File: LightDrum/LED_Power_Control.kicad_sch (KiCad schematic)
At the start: 9 parts, among them J901 DIN-4-SH, K901 ALQ112, K902 ALQ112, U902 SSM3K361R_SOT23F

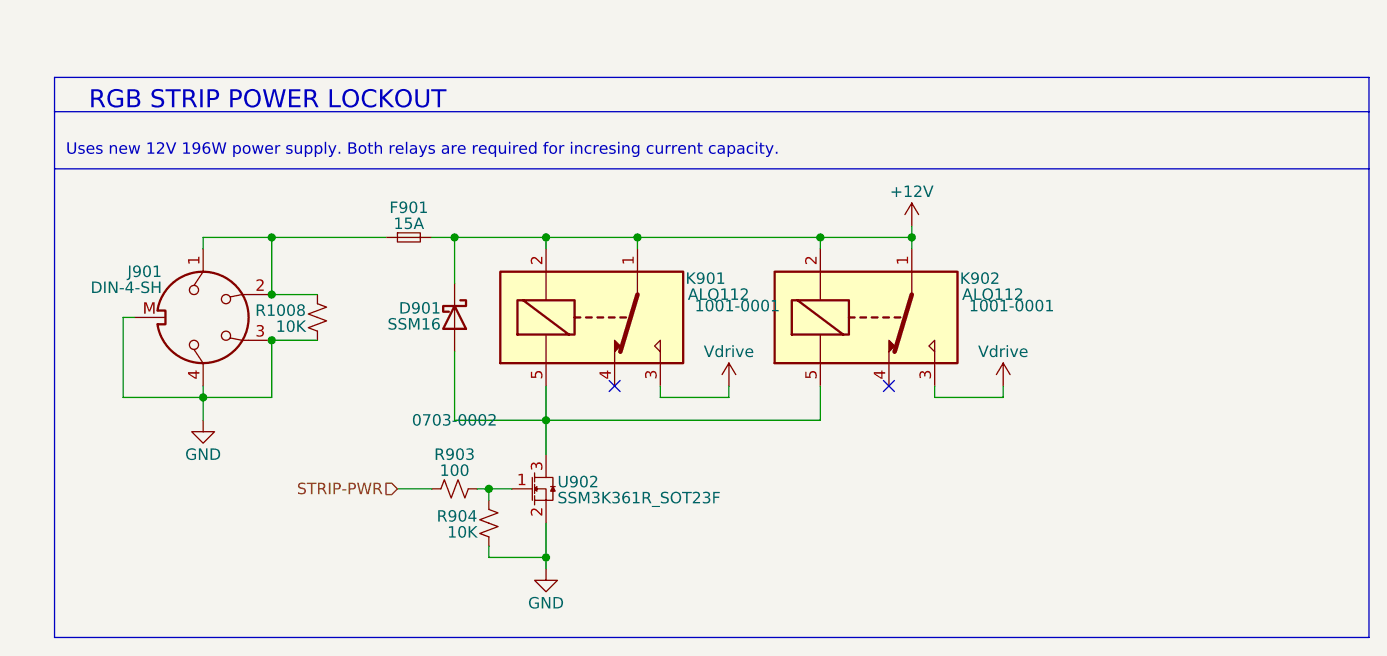
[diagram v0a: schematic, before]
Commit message: Replace relays and SWD conn
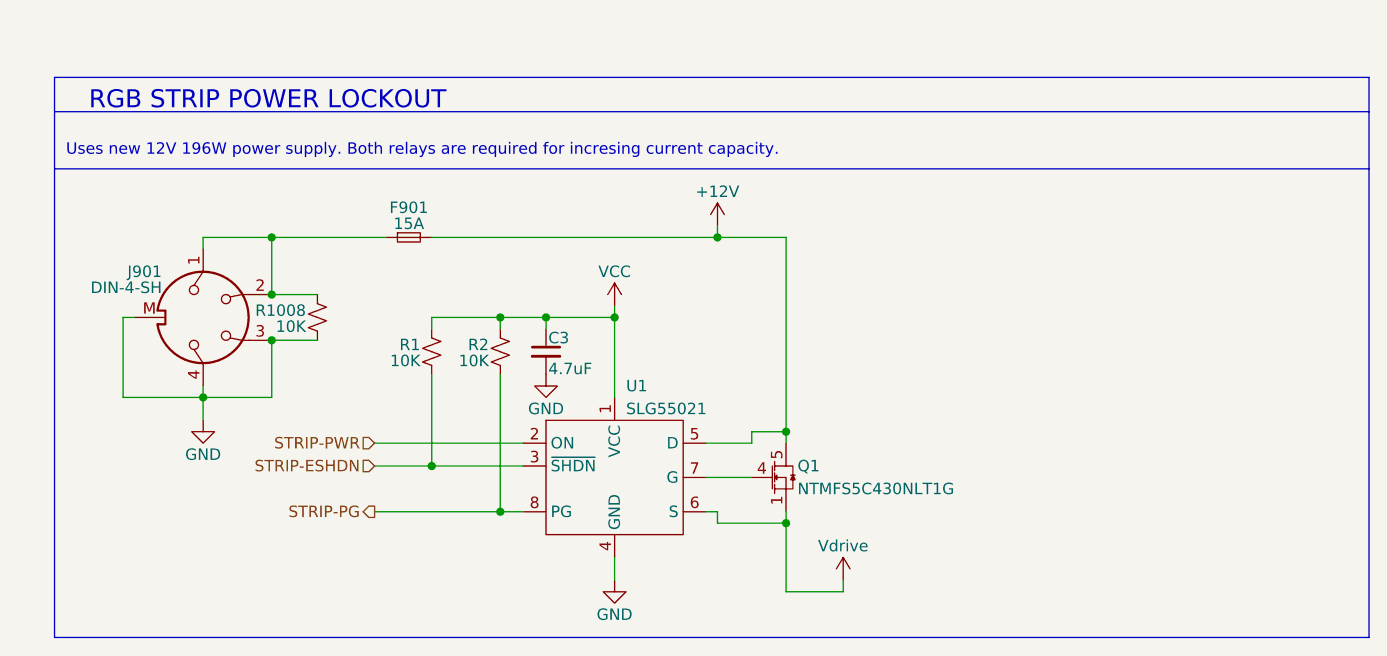
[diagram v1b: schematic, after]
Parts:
- removed D901: SSM16, Diode_SMD:D_SOD-323_HandSoldering, symbol Device:D_Schottky
- removed K901, K902: ALQ112, Daxxn_Relays:ALQ112, symbol Daxxn_Relays:ALQ112
- removed R903: 100, Resistor_SMD:R_0805_2012Metric, symbol Device:R_Small_US
- removed R904: 10K, Resistor_SMD:R_0805_2012Metric, symbol Device:R_Small_US
- removed U902: SSM3K361R_SOT23F, Package_TO_SOT_SMD:SOT-23, symbol Daxxn_Transistors:SSM3K361R_SOT23F
- added C3: 4.7uF, Capacitor_SMD:C_0805_2012Metric, symbol Daxxn_Device:C
- added Q1: NTMFS5C430NLT1G, Daxxn_Packages:POWER-FET-5-DFN, symbol Daxxn_Transistors:NTMFS5C430NL
- added R1, R2: 10K, Resistor_SMD:R_0402_1005Metric, symbol Device:R_Small_US
- added U1: SLG55021, Package_DFN_QFN:TDFN-8-1EP_2x2mm_P0.5mm_EP0.8x1.2mm, symbol Daxxn_IC:SLG55021
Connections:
- net +12V: now also Q1.5 (D), U1.5 (D)
- net GND: now also C3.2, U1.4 (GND), U1.9 (GND)
- net STRIP-PWR: now also U1.2 (ON)
- net Vdrive: now also Q1.1 (S), Q1.2 (S), Q1.3 (S), U1.6 (S)
- new net: Q1.4 (G), U1.7 (G)
- new net STRIP-ESHDN: R1.2, U1.3 (~{SHDN})
- new net STRIP-PG: R2.2, U1.8 (PG)
- new net VCC: C3.1, R1.1, R2.1, U1.1 (VCC)
- no-connect marks 2 -> 0

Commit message: Preliminary schematic lock - Starting PCB layout
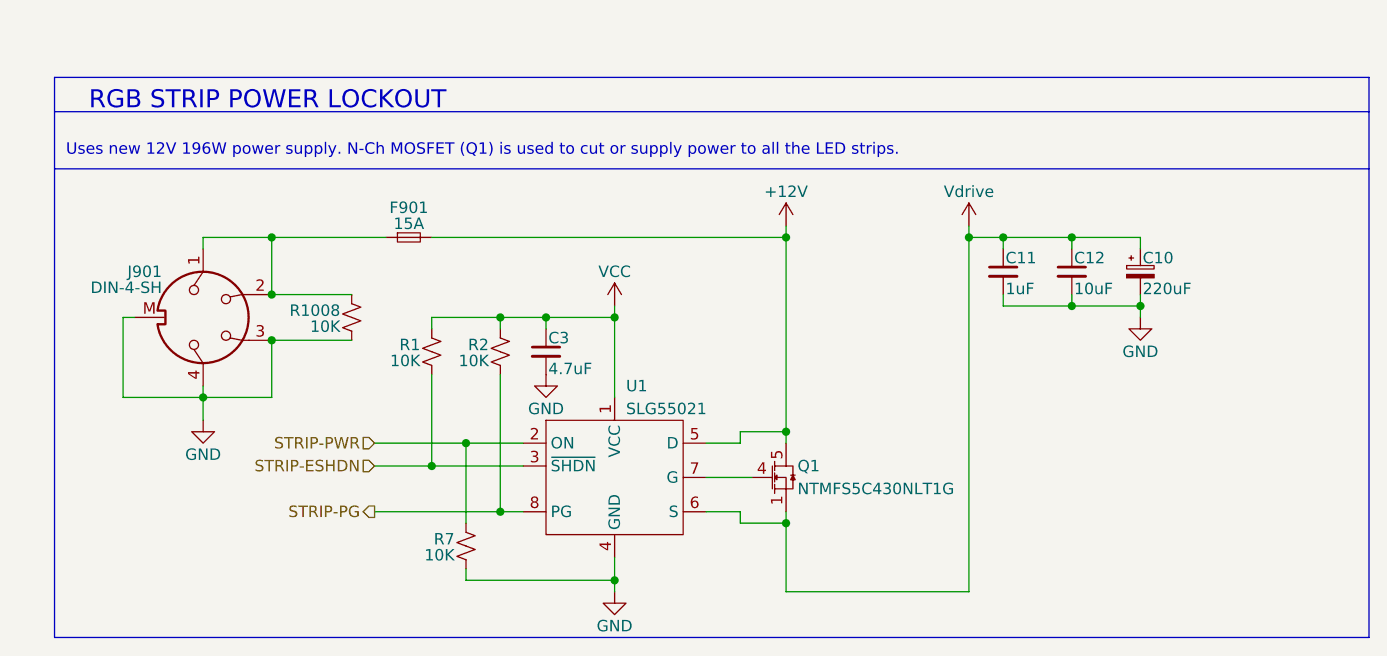
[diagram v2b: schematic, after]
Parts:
- added C10: 220uF, Capacitor_SMD:CP_Elec_8x10, symbol Daxxn_Device:C_Pol
- added C11: 1uF, Capacitor_SMD:C_0603_1608Metric, symbol Daxxn_Device:C
- added C12: 10uF, Capacitor_SMD:C_1210_3225Metric, symbol Daxxn_Device:C
- added R7: 10K, Resistor_SMD:R_0402_1005Metric, symbol Device:R_Small_US
- C3: SupplierPN (none) -> 1276-6722-1-ND
- F901: SupplierPN (none) -> 36-3557-10-ND
- J901: SupplierPN (none) -> 2092-KPJXHT-4S-S-ND
- Q1: SupplierPN (none) -> NTMFS5C430NLT1GOSCT-ND
- R1, R2: SupplierPN (none) -> 311-10KJRCT-ND
- R1008: SupplierPN (none) -> 13-RE1206FRE0710KLCT-ND
- U1: SupplierPN (none) -> 1827-1047-1-ND
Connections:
- net GND: now also C10.2, C11.2, C12.2, R7.2
- net STRIP-PWR: now also R7.1
- net Vdrive: now also C10.1, C11.1, C12.1
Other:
- note added: "Uses new 12V 196W power supply. N-Ch MOSFET (Q1) is used to cut or supply power to all the LED strips."
- note removed: "Uses new 12V 196W power supply. Both relays are required for incresing current capacity."
- moved on the sheet: R1008

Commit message: Component placement complete
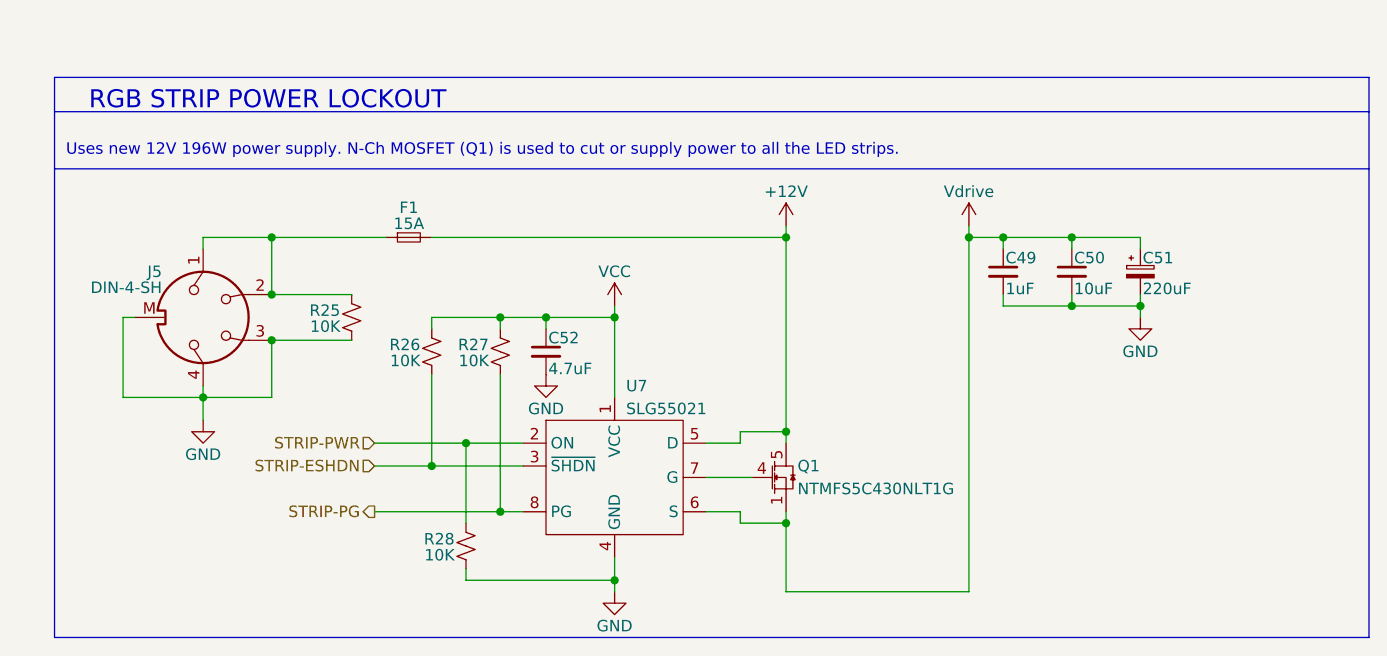
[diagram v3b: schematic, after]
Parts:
- U7: renamed from U1; footprint Package_DFN_QFN:TDFN-8-1EP_2x2mm_P0.5mm_EP0.8x1.2mm -> Daxxn_Packages:TDFN-8-1EP_2x2mm_P0.5mm_EP0.8x1.2mm
- renumbered C11 to C49, C12 to C50, C10 to C51, C3 to C52, F901 to F1, J901 to J5, R1008 to R25, R1 to R26, R2 to R27, R7 to R28

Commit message: Replace DSub with much better ECU conn
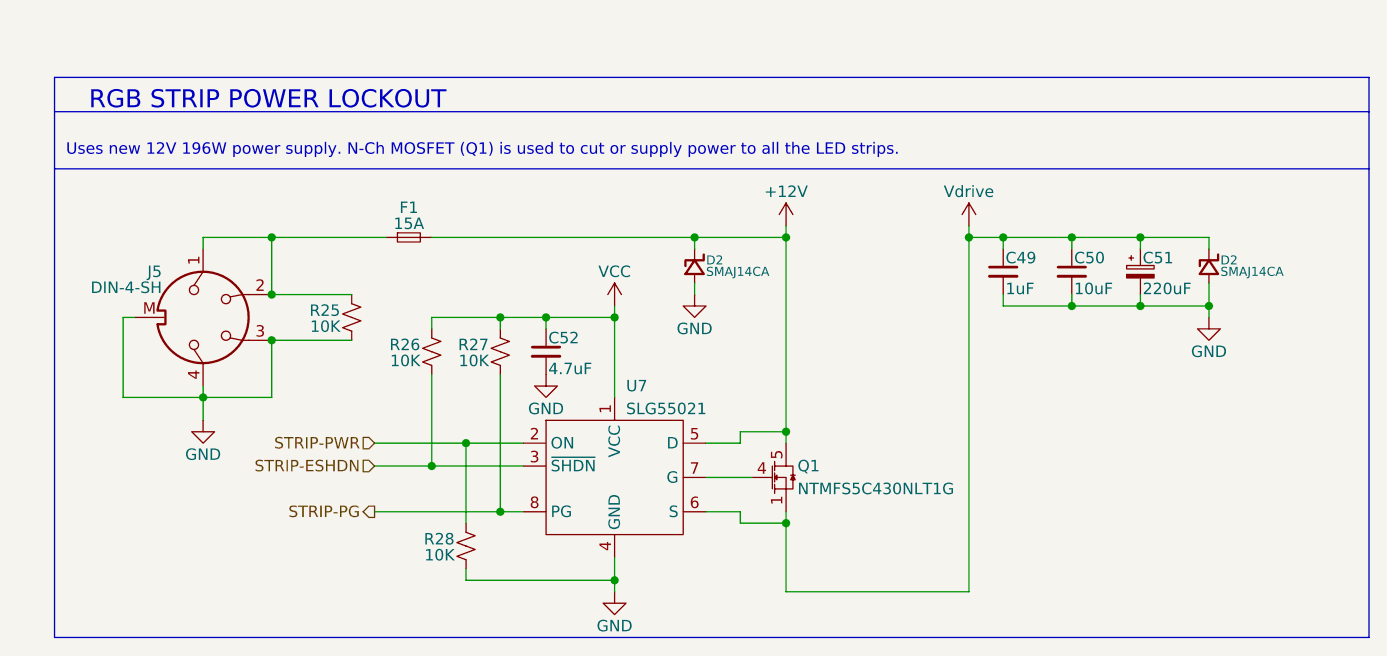
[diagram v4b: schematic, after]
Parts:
- added D2 (x2): SMAJ14CA, Diode_SMD:D_SMA, symbol Daxxn_Device:D_TVS_U
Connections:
- net +12V: now also D2.1 (K)
- net GND: now also D2.2 (A), D2.2 (A)
- net Vdrive: now also D2.1 (K)
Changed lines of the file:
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@@
   (junction (at 58.42 62.23) (diameter 0) (color 0 0 0 0)
   )
+  (junction (at 144.78 44.45) (diameter 0) (color 0 0 0 0)
+  )
+  (junction (at 137.16 36.83) (diameter 0) (color 0 0 0 0)
+  )
   (junction (at 97.79 58.42) (diameter 0) (color 0 0 0 0)
   )
@@
   (junction (at 71.12 45.72) (diameter 0) (color 0 0 0 0)
   )
+  (junction (at 87.63 36.83) (diameter 0) (color 0 0 0 0)
+  )
   (junction (at 129.54 44.45) (diameter 0) (color 0 0 0 0)
   )
@@
     (stroke (width 0) (type default))
   )
+  (wire (pts (xy 144.78 41.91) (xy 144.78 44.45))
+    (stroke (width 0) (type default))
+  )
   (wire (pts (xy 118.11 35.56) (xy 118.11 36.83))
     (stroke (width 0) (type default))
@@
     (stroke (width 0) (type default))
   )
+  (wire (pts (xy 87.63 41.91) (xy 87.63 43.18))
+    (stroke (width 0) (type default))
+  )
   (wire (pts (xy 92.71 58.42) (xy 97.79 58.42))
     (stroke (width 0) (type default))
@@
     (stroke (width 0) (type default))
   )
+  (wire (pts (xy 87.63 36.83) (xy 97.79 36.83))
+    (stroke (width 0) (type default))
+  )
   (wire (pts (xy 62.23 59.69) (xy 62.23 68.58))
     (stroke (width 0) (type default))
@@
     (stroke (width 0) (type default))
   )
+  (wire (pts (xy 87.63 36.83) (xy 87.63 38.1))
+    (stroke (width 0) (type default))
+  )
   (wire (pts (xy 129.54 44.45) (xy 137.16 44.45))
     (stroke (width 0) (type default))
@@
     (stroke (width 0) (type default))
   )
+  (wire (pts (xy 144.78 38.1) (xy 144.78 36.83))
+    (stroke (width 0) (type default))
+  )
   (wire (pts (xy 33.02 38.1) (xy 33.02 36.83))
     (stroke (width 0) (type default))
   )
+  (wire (pts (xy 144.78 36.83) (xy 137.16 36.83))
+    (stroke (width 0) (type default))
+  )
+  (wire (pts (xy 144.78 44.45) (xy 137.16 44.45))
+    (stroke (width 0) (type default))
+  )
   (wire (pts (xy 92.71 67.31) (xy 88.9 67.31))
     (stroke (width 0) (type default))
@@
     (stroke (width 0) (type default))
   )
-  (wire (pts (xy 137.16 44.45) (xy 137.16 45.72))
-    (stroke (width 0) (type default))
-  )
-  (wire (pts (xy 58.42 36.83) (xy 97.79 36.83))
+  (wire (pts (xy 144.78 44.45) (xy 144.78 45.72))
+    (stroke (width 0) (type default))
+  )
+  (wire (pts (xy 58.42 36.83) (xy 87.63 36.83))
     (stroke (width 0) (type default))
   )
@@
     )
   )
+  (symbol (lib_id "Daxxn_Device:D_TVS_U") (at 87.63 39.37 270) (unit 1)
+    (in_bom yes) (on_board yes) (dnp no)
+    (property "Reference" "D2" (at 88.9 39.37 90)
+      (effects (font (size 1 1)) (justify left))
+    )
+    (property "Value" "SMAJ14CA" (at 88.9 40.64 90)
+      (effects (font (size 1 1)) (justify left))
+    )
+    (property "Footprint" "Diode_SMD:D_SMA" (at 87.63 40.132 90)
+      (effects (font (size 1.27 1.27)) hide)
+    )
+    (property "Datasheet" "~" (at 85.471 39.37 90)
+      (effects (font (size 1.27 1.27)) hide)
+    )
+    (property "Schematic" "" (at 87.63 39.37 0)
+      (effects (font (size 1.27 1.27)) hide)
+    )
+    (property "PartNumber" "" (at 87.63 39.37 0)
+      (effects (font (size 1.27 1.27)))
+    )
+    (property "SupplierPN" "SMAJ14CA-FDICT-ND" (at 87.63 39.37 0)
+      (effects (font (size 1.27 1.27)) hide)
+    )
+    (pin "1")
+    (pin "2")
+    (instances
+      (project "LightDrum"
+        (path "/7f137461-fd46-4a4c-8db7-555d487fb3ca/0b4455a9-9524-4969-89d6-fafc6f740fef"
+          (reference "D2") (unit 1)
+        )
+        (path "/7f137461-fd46-4a4c-8db7-555d487fb3ca/c5b6f44f-b454-4d73-ae8d-4f0249b04054/75c45b3d-e09a-41c7-88e5-ae1bbc637da8"
+          (reference "D9") (unit 1)
+        )
+        (path "/7f137461-fd46-4a4c-8db7-555d487fb3ca/1cf17c4e-5921-408b-a9f8-9e373eae7d69/33823fd6-c5f7-46ac-ae5c-a135891f46f0"
+          (reference "D9") (unit 1)
+        )
+      )
+    )
+  )
   (symbol (lib_id "Device:R_Small_US") (at 58.42 49.53 0) (unit 1)
     (in_bom yes) (on_board yes) (dnp no)
@@
     )
   )
+  (symbol (lib_id "Daxxn_Device:D_TVS_U") (at 144.78 39.37 270) (unit 1)
+    (in_bom yes) (on_board yes) (dnp no)
+    (property "Reference" "D2" (at 146.05 39.37 90)
+      (effects (font (size 1 1)) (justify left))
+    )
+    (property "Value" "SMAJ14CA" (at 146.05 40.64 90)
+      (effects (font (size 1 1)) (justify left))
+    )
+    (property "Footprint" "Diode_SMD:D_SMA" (at 144.78 40.132 90)
+      (effects (font (size 1.27 1.27)) hide)
+    )
+    (property "Datasheet" "~" (at 142.621 39.37 90)
+      (effects (font (size 1.27 1.27)) hide)
+    )
+    (property "Schematic" "" (at 144.78 39.37 0)
+      (effects (font (size 1.27 1.27)) hide)
+    )
+    (property "PartNumber" "" (at 144.78 39.37 0)
+      (effects (font (size 1.27 1.27)))
+    )
+    (property "SupplierPN" "SMAJ14CA-FDICT-ND" (at 144.78 39.37 0)
+      (effects (font (size 1.27 1.27)) hide)
+    )
+    (pin "1")
+    (pin "2")
+    (instances
+      (project "LightDrum"
+        (path "/7f137461-fd46-4a4c-8db7-555d487fb3ca/0b4455a9-9524-4969-89d6-fafc6f740fef"
+          (reference "D2") (unit 1)
+        )
+        (path "/7f137461-fd46-4a4c-8db7-555d487fb3ca/c5b6f44f-b454-4d73-ae8d-4f0249b04054/75c45b3d-e09a-41c7-88e5-ae1bbc637da8"
+          (reference "D8") (unit 1)
+        )
+        (path "/7f137461-fd46-4a4c-8db7-555d487fb3ca/1cf17c4e-5921-408b-a9f8-9e373eae7d69/33823fd6-c5f7-46ac-ae5c-a135891f46f0"
+          (reference "D8") (unit 1)
+        )
+      )
+    )
+  )
   (symbol (lib_id "Device:Fuse_Small") (at 55.88 36.83 0) (unit 1)
     (in_bom yes) (on_board yes) (dnp no)
@@
         (path "/7f137461-fd46-4a4c-8db7-555d487fb3ca/1cf17c4e-5921-408b-a9f8-9e373eae7d69/33823fd6-c5f7-46ac-ae5c-a135891f46f0"
           (reference "F1") (unit 1)
+        )
+      )
+    )
+  )
+  (symbol (lib_id "power:GND") (at 87.63 43.18 0) (unit 1)
+    (in_bom yes) (on_board yes) (dnp no)
+    (property "Reference" "#PWR094" (at 87.63 49.53 0)
+      (effects (font (size 1.27 1.27)) hide)
+    )
+    (property "Value" "GND" (at 87.63 46.99 0)
+      (effects (font (size 1.27 1.27)))
+    )
+    (property "Footprint" "" (at 87.63 43.18 0)
+      (effects (font (size 1.27 1.27)) hide)
+    )
+    (property "Datasheet" "" (at 87.63 43.18 0)
+      (effects (font (size 1.27 1.27)) hide)
+    )
+    (pin "1")
+    (instances
+      (project "LightDrum"
+        (path "/7f137461-fd46-4a4c-8db7-555d487fb3ca/1cf17c4e-5921-408b-a9f8-9e373eae7d69/33823fd6-c5f7-46ac-ae5c-a135891f46f0"
+          (reference "#PWR094") (unit 1)
         )
       )
@@
     )
   )
-  (symbol (lib_id "power:GND") (at 137.16 45.72 0) (unit 1)
-    (in_bom yes) (on_board yes) (dnp no)
-    (property "Reference" "#PWR056" (at 137.16 52.07 0)
-      (effects (font (size 1.27 1.27)) hide)
-    )
-    (property "Value" "GND" (at 137.16 49.53 0)
-      (effects (font (size 1.27 1.27)))
-    )
-    (property "Footprint" "" (at 137.16 45.72 0)
-      (effects (font (size 1.27 1.27)) hide)
-    )
-    (property "Datasheet" "" (at 137.16 45.72 0)
-      (effects (font (size 1.27 1.27)) hide)
-    )
+  (symbol (lib_id "power:GND") (at 144.78 45.72 0) (unit 1)
+    (in_bom yes) (on_board yes) (dnp no)
+    (property "Reference" "#PWR056" (at 144.78 52.07 0)
+      (effects (font (size 1.27 1.27)) hide)
+    )
+    (property "Value" "GND" (at 144.78 49.53 0)
+      (effects (font (size 1.27 1.27)))
+    )
+    (property "Footprint" "" (at 144.78 45.72 0)
+      (effects (font (size 1.27 1.27)) hide)
+    )
+    (property "Datasheet" "" (at 144.78 45.72 0)
+      (effects (font (size 1.27 1.27)) hide)
+    )

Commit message: Fix schematic layout
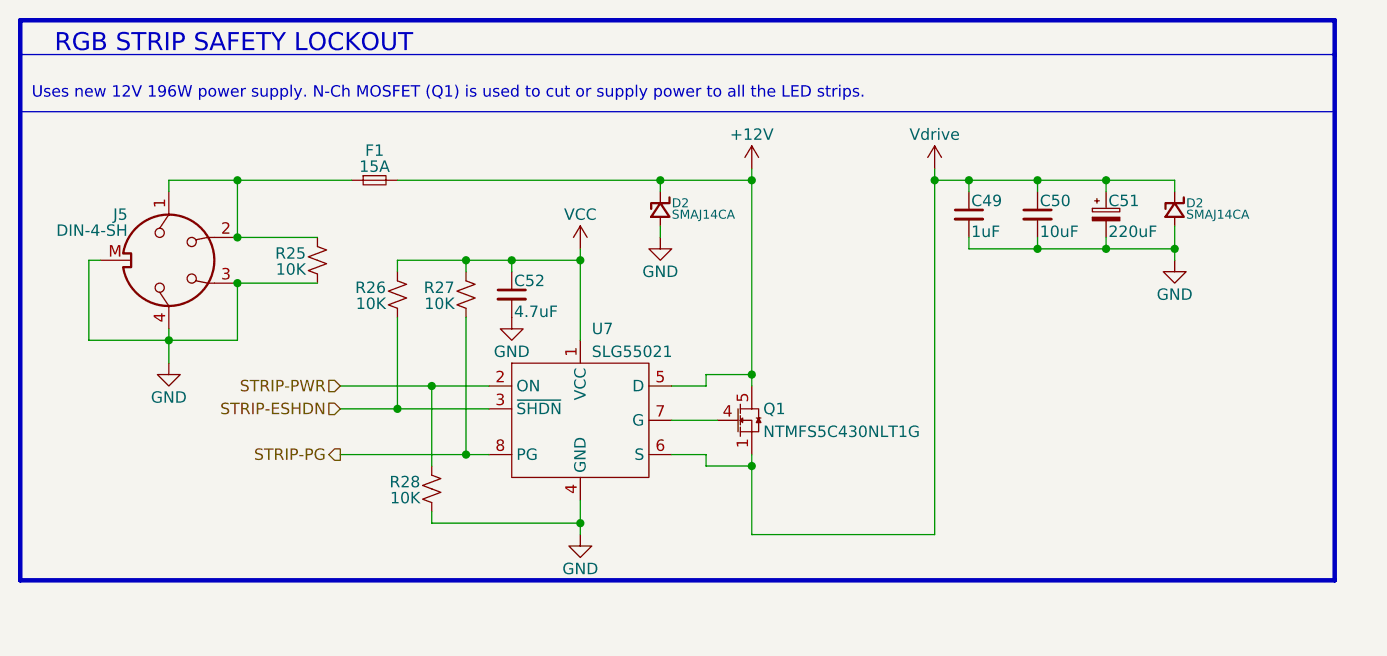
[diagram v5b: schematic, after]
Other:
- note added: "RGB STRIP SAFETY LOCKOUT"
- note removed: "RGB STRIP POWER LOCKOUT"
- moved on the sheet: C49, C50, C51, C52, D2, F1, J5, Q1, R25, R26, R27, R28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
